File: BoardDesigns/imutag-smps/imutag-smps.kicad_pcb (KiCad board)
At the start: 4 copper layers, 21.5 x 11.5 mm, 37 parts, among them J201 CONN_02X04, J301 Conn_01x01, J302 Conn_01x01, J303 Conn_01x01, J304 Conn_01x01, J401 CONN_01X02, Q501 PMBT2222AMBYL, U1 TPS22916BYFPR, U2 BMM350, U3 BMP581, U302 stm32U375, U4 TPS7A02185PDQNR, U5 LSM6DSV16X, U501 RV-3028-C8, U6 GD5F1GQ5REYIGR

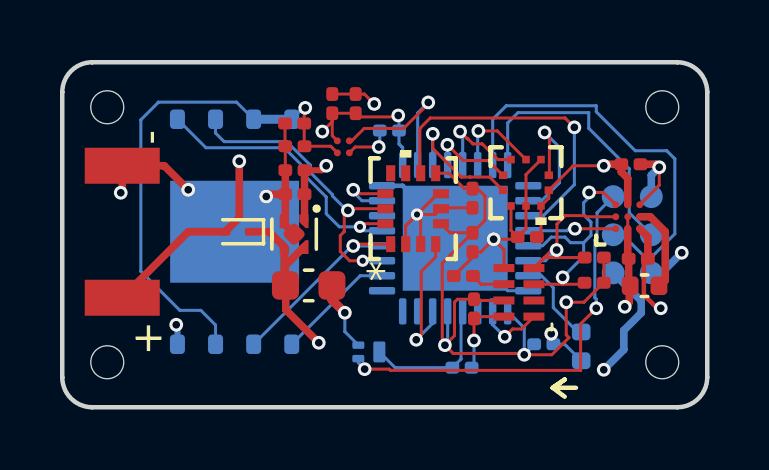
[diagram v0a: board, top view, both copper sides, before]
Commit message: added imutag-smps and imutag plastic
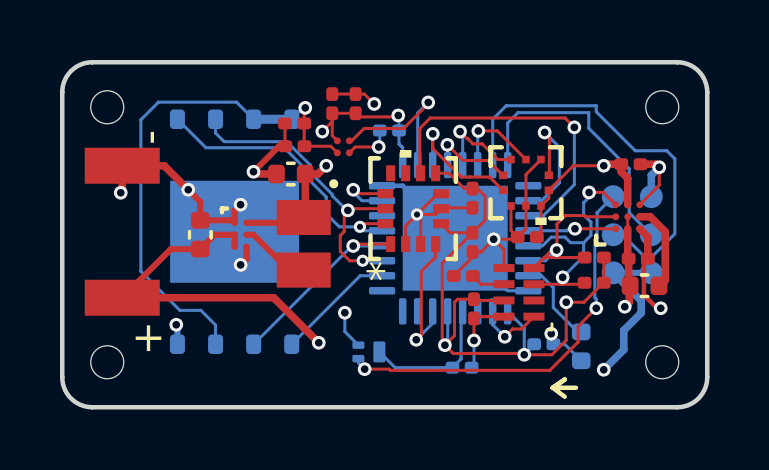
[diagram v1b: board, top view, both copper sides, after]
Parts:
- removed C9: 0.1uf, Capacitor_SMD:C_0201_0603Metric
- removed D401: D, Diode_SMD:D_SOD-923
- added L1: 2.2uH, libraries:IND_DFE2016_MUR, F.Cu at (148.1, 107.6)
- C7: value 10uf -> 4.7uf; footprint Capacitor_SMD:C_0603_1608Metric -> Capacitor_SMD:C_0402_1005Metric
- C8: value 1uf -> 10uf; footprint Capacitor_SMD:C_0201_0603Metric -> Capacitor_SMD:C_0402_1005Metric
- U4: value TPS7A02185PDQNR -> TPS62840YBGR; footprint Package_SON:Texas_X2SON-4_1x1mm_P0.65mm -> libraries:DSBGA6_1P4XP9_TEX
- U6: value GD5F1GQ5REYIGR -> GD5F2GM7REYIGR
- moved C7 3.99 mm to (144.6, 107.2), turned to 90 degrees
- moved U4 1.79 mm to (145.9, 107.2), turned to 0 degrees
- moved C8 0.69 mm to (147.6, 105.2)
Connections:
- C7 pad 1: VIN -> VBAT
- J201 pad 1: VIN -> VBAT
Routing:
- net VIN: track 20.2 -> 0.00 mm, vias 2 -> 0
- net Net-(U4-SW): track 0.00 -> 3.09 mm
- net +1V8: track 40.9 -> 42.6 mm
- net VBAT: track 28.9 -> 27.5 mm
- net GND: track 48.9 -> 50.0 mm, vias 13 -> 15
- net RST: track 14.0 -> 13.4 mm

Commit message: update plastic designs
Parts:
- moved C7 4.27 mm to (147.1, 110.7), turned to 180 degrees
- moved U4 2.41 mm to (147.1, 109.4), turned to 90 degrees
- moved L1 0.73 mm to (147.4, 107.3), turned to 0 degrees
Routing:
- net +1V8: track 42.6 -> 43.6 mm
- net Net-(U4-SW): track 3.09 -> 2.21 mm
- net VBAT: track 27.5 -> 27.9 mm, vias 2 -> 3
- net GND: track 50.0 -> 50.3 mm, vias 15 -> 17
- added copper zone on F.Cu, net GND
- added copper zone on F.Cu, net VBAT

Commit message: ran design review on imutag-smps
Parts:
- U5: value LSM6DSV16X -> LSM6DSV
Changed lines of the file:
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@@
 		(embedded_fonts no)
 		(model "${TAG_LIBRARIES}/packages3D/lipo.step"
+			(hide yes)
 			(offset
 				(xyz 0 -1 0.5)
@@
 			)
 		)
-		(property "Value" "LSM6DSV16X"
+		(property "Value" "LSM6DSV"
 			(at 0 0 90)
 			(unlocked yes)
@@
 			)
 		)
-		(property "Datasheet" "LSM6DSV16X"
+		(property "Datasheet" "LSM6DSV"
 			(at 0 0 90)
 			(unlocked yes)
@@
 			)
 		)
-		(property "MFN" "STMicroelectronics"
+		(property "MFN" "STM microelectronics"
 			(at 0 0 90)
 			(unlocked yes)
@@
 			)
 		)
-		(property "MPN" "LSM6DSV16XTR"
+		(property "MPN" "LSM6DSV"
 			(at 0 0 90)
 			(unlocked yes)
@@
 			)
 		)
-		(property "LCSC" "C5267406"
+		(property "LCSC" "C5267399"
 			(at 0 0 90)
 			(unlocked yes)

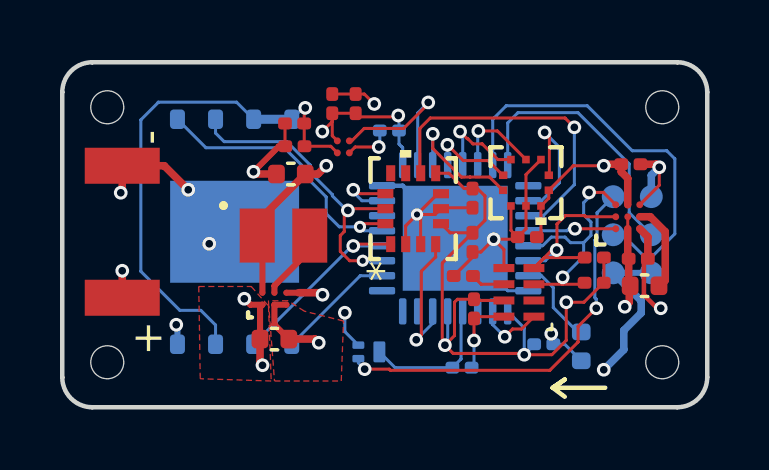
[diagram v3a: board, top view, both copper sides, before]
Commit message: added design review
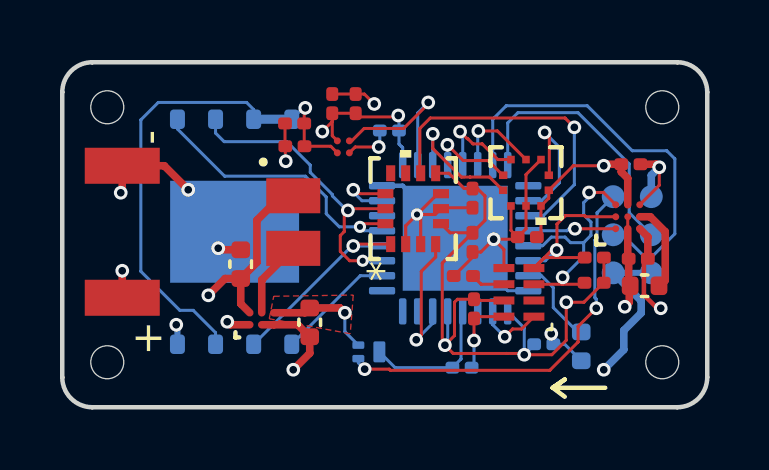
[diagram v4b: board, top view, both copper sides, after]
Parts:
- moved C8 3.44 mm to (145.9, 108.2), turned to 90 degrees
- moved C7 1.30 mm to (148.2, 110.2), turned to 90 degrees
- moved U4 0.79 mm to (146.7, 110.0)
- moved L1 0.56 mm to (147.7, 106.8), turned to -90 degrees
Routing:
- net GND: track 50.3 -> 48.6 mm, vias 17 -> 15
- net +1V8: track 43.6 -> 44.6 mm
- removed copper zone on F.Cu, net VBAT
